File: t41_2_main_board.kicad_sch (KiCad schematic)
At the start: 18 parts, among them IC1 74HC125D, J1 Conn_02x08_Odd_Even, J2 Conn_02x05_Odd_Even, J3 Conn_02x05_Odd_Even, J4 Conn_02x05_Odd_Even, J5 Conn_02x05_Odd_Even, J6 SJ-3524-SMT, J7 SJ-3524-SMT, J8 SJ-3524-SMT, U1 Teensy4.1

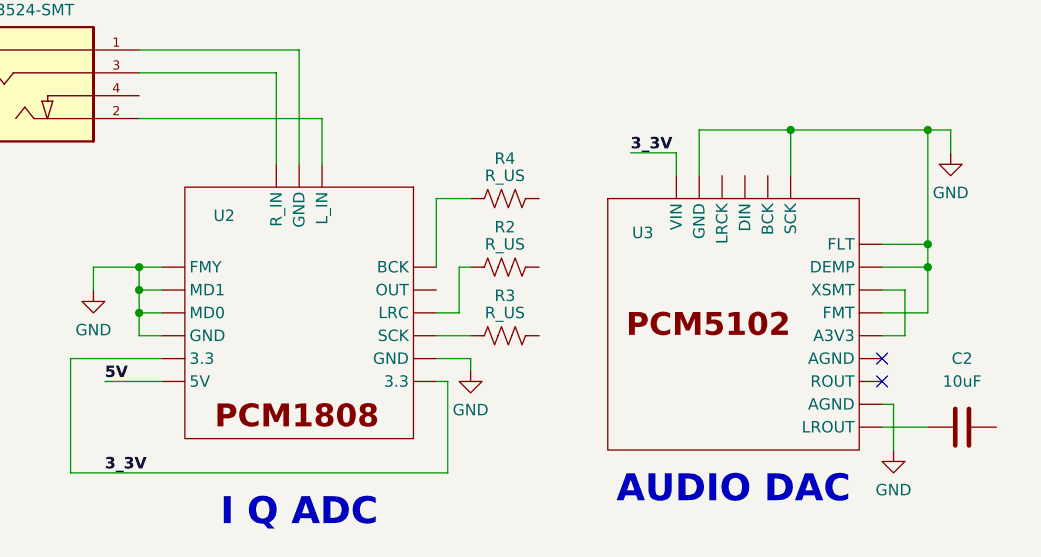
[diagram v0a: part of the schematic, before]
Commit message: Built footprints for data converters.
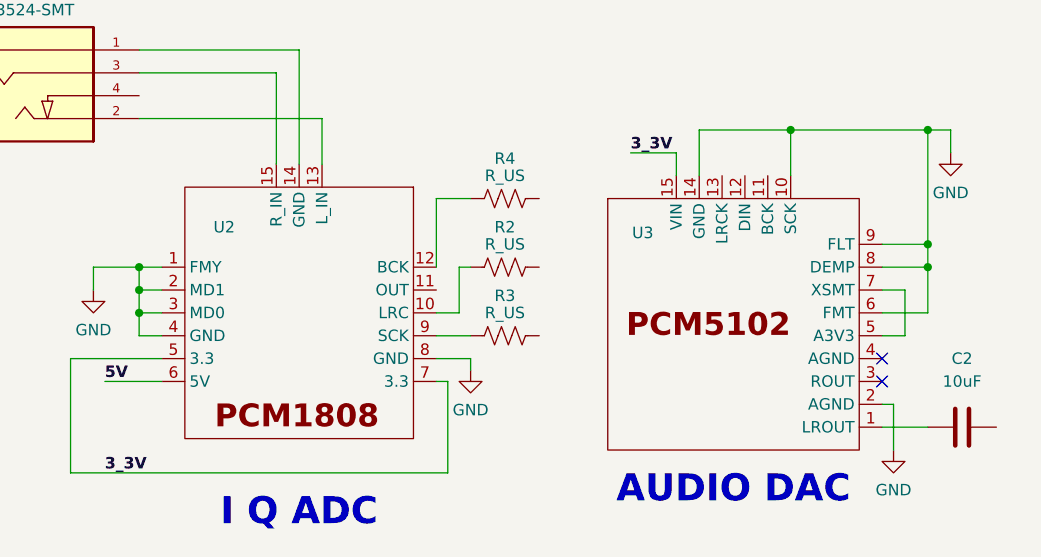
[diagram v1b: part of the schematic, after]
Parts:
- U1: footprint (none) -> teensy:Teensy41
- U2: footprint (none) -> PCM1808_module:PCM1808_module
- U3: footprint (none) -> PCM5102_module:PCM5102_module
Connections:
- net 3_3V: now also U2.5 (3.3), U2.7 (3.3), U3.15 (VIN); no longer U2. (SCK), U3. (XSMT)
- net 5V: now also U2.6 (5V); no longer U2. (SCK)
- net GND: now also U2.1 (FMY), U2.2 (MD1), U2.3 (MD0), U2.4 (GND), U2.8 (GND), U3.10 (SCK), U3.14 (GND), U3.2 (AGND), U3.6 (FMT), U3.8 (DEMP), U3.9 (FLT); no longer U2. (SCK), U3. (XSMT)
- net at R2.1: now also U2.10 (LRC); no longer U2. (SCK)
- net at J6.1: now also U2.14 (GND); no longer U2. (SCK)
- net at J6.2: now also U2.13 (L_IN); no longer U2. (SCK)
- net at J6.3: now also U2.15 (R_IN); no longer U2. (SCK)
- net at C2.1: now also U3.1 (LROUT); no longer U3. (XSMT)
- net at R4.1: now also U2.12 (BCK); no longer U2. (SCK)
- net at R3.1: now also U2.9 (SCK); no longer U2. (SCK)
- new net: U3.5 (A3V3), U3.7 (XSMT)
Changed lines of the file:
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@@
 			)
 		)
-		(property "Footprint" ""
+		(property "Footprint" "teensy:Teensy41"
 			(at 81.28 95.25 0)
 			(effects
@@
 			)
 		)
-		(property "Footprint" ""
+		(property "Footprint" "PCM5102_module:PCM5102_module"
 			(at 111.76 178.435 0)
 			(effects
@@
 			)
 		)
-		(pin ""
-		)
-		(pin ""
-		)
-		(pin ""
-		)
-		(pin ""
-		)
-		(pin ""
-		)
-		(pin ""
-		)
-		(pin ""
-		)
-		(pin ""
-		)
-		(pin ""
-		)
-		(pin ""
-		)
-		(pin ""
-		)
-		(pin ""
-		)
-		(pin ""
-		)
-		(pin ""
-		)
-		(pin ""
+		(pin "1"
+		)
+		(pin "3"
+		)
+		(pin "13"
+		)
+		(pin "2"
+		)
+		(pin "14"
+		)
+		(pin "11"
+		)
+		(pin "6"
+		)
+		(pin "7"
+		)
+		(pin "12"
+		)
+		(pin "4"
+		)
+		(pin "5"
+		)
+		(pin "10"
+		)
+		(pin "15"
+		)
+		(pin "9"
+		)
+		(pin "8"
 		)
 		(instances
@@
 	(symbol
 		(lib_id "PCM1808_module:PCM1808_module")
-		(at 63.5 178.435 270)
+		(at 63.5 177.165 0)
 		(unit 1)
 		(exclude_from_sim no)
@@
 		(dnp no)
 		(property "Reference" "U2"
-			(at 53.975 166.37 90)
+			(at 53.975 167.64 0)
 			(effects
 				(font
@@
 		)
 		(property "Value" "~"
-			(at 67.31 212.725 0)
+			(at 97.79 173.355 0)
 			(effects
 				(font
@@
 			)
 		)
-		(property "Footprint" ""
-			(at 63.5 178.435 0)
+		(property "Footprint" "PCM1808_module:PCM1808_module"
+			(at 63.5 177.165 0)
 			(effects
 				(font
@@
 		)
 		(property "Datasheet" ""
-			(at 63.5 178.435 0)
+			(at 63.5 177.165 0)
 			(effects
 				(font
@@
 		)
 		(property "Description" ""
-			(at 63.5 178.435 0)
-			(effects
-				(font
-					(size 1.27 1.27)
-				)
-				(hide yes)
-			)
-		)
-		(pin ""
-		)
-		(pin ""
-		)
-		(pin ""
-		)
-		(pin ""
-		)
-		(pin ""
-		)
-		(pin ""
-		)
-		(pin ""
-		)
-		(pin ""
-		)
-		(pin ""
-		)
-		(pin ""
-		)
-		(pin ""
-		)
-		(pin ""
-		)
-		(pin ""
-		)
-		(pin ""
-		)
-		(pin ""
-		)
-		(instances
+			(at 63.5 177.165 0)
+			(effects
+				(font
+					(size 1.27 1.27)
+				)
+				(hide yes)
+			)
+		)
+		(pin "4"
+		)
+		(pin "7"
+		)
+		(pin "1"
+		)
+		(pin "14"
+		)
+		(pin "9"
+		)
+		(pin "2"
+		)
+		(pin "11"
+		)
+		(pin "15"
+		)
+		(pin "5"
+		)
+		(pin "6"
+		)
+		(pin "3"
+		)
+		(pin "10"
+		)
+		(pin "8"
+		)
+		(pin "13"
+		)
+		(pin "12"
+		)
+		(instances

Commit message: Schematic nearing completion.
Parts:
- added C10, C11, C12, C13, C14, C15, C3, C7, C8, C9: 470pF, symbol Device:C_Small
- added C4, C5, C6: C_Small, symbol Device:C_Small
- added FB1, FB2, FB3, FB4, FB5: FerriteBead, symbol Device:FerriteBead_Small
- added J10, J12: SJ-3524-SMT, Connector_Audio:Jack_3.5mm_CUI_SJ-3524-SMT_Horizontal, symbol SJ-3524-SMT:SJ-3524-SMT
- added J11: B2B-XH-A_LF__SN_, digikey-footprints:PinHeader_1x2_P2.5mm_Drill1.1mm, symbol dk_Rectangular-Connectors-Headers-Male-Pins:B2B-XH-A_LF__SN_
- added J13, J9: B3B-XH-A_LF__SN_, digikey-footprints:PinHeader_1x3_P2.5mm_Drill1.1mm, symbol dk_Rectangular-Connectors-Headers-Male-Pins:B3B-XH-A_LF__SN_
- added J15: B4B-XH-A_LF__SN_, digikey-footprints:PinHeader_1x4_P2.5mm_Drill1.1mm, symbol dk_Rectangular-Connectors-Headers-Male-Pins:B4B-XH-A_LF__SN_
- IC1: footprint SOIC14 -> Package_SO:SOIC-14_3.9x8.7mm_P1.27mm
- J1: footprint (none) -> Connector_IDC:IDC-Header_2x08_P2.54mm_Vertical
- J2, J3, J4, J5: footprint (none) -> Connector_IDC:IDC-Header_2x05_P2.54mm_Vertical
- J6, J7, J8: footprint CUI_SJ-3524-SMT -> Connector_Audio:Jack_3.5mm_CUI_SJ-3524-SMT_Horizontal
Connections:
- net 5V is gone; now on net 5V_FIL: U2.6 (5V)
- net CS: now also U1.12 (10_CS_MQSR)
- net GND: now also J2.1 (Pin_1), J2.2 (Pin_2), J3.9 (Pin_9), J4.1 (Pin_1), J4.2 (Pin_2), J6.1, J8.1, U1.34 (GND), U1.47 (GND), U2.14 (GND), C3.2, C4.2, C5.2, C6.2, C7.1, C8.1, J10.1, J12.1, J13.2
- net MISO: now also IC1.6, U1.14 (12_MISO_MQSL)
- net MOSI: now also U1.13 (11_MOSI_CTX1); no longer IC1.3, J5.4 (Pin_4)
- net at J4.5 (Pin_5): now also U1.38 (16_A2_RX4_SCL1)
- net at J4.6 (Pin_6): now also U1.36 (14_A0_TX3_SPDIF_OUT)
- net at J4.7 (Pin_7): now also U1.39 (17_A3_TX4_SDA1)
- net at J4.8 (Pin_8): now also U1.37 (15_A1_RX3_SPDIF_IN)
- net at J7.1: now also J9.2
- net at J7.2: now also J9.1
- net at J7.3: now also J9.3
- net at J8.2: now also J11.1
- net at J8.3: now also J11.2
- net RESET: now reaches J1.1 (Pin_1)
- net RESET: now also U1.2 (0_RX1_CRX2_CS1)
- net 5V_IN: now reaches J1.10 (Pin_10)
- net 5V_IN: now also J1.9 (Pin_9), FB2.1
- net TXRX: now reaches J1.2 (Pin_2)
- net SDA: now reaches J1.3 (Pin_3)
- net SDA: now also J3.7 (Pin_7), U1.40 (18_A4_SDA)
- net SCL: now reaches J1.4 (Pin_4)
- net SCL: now also J3.8 (Pin_8), U1.41 (19_A5_SCL)
- net 12V_IN: now reaches J1.5 (Pin_5)
- net 12V_IN: now also J1.6 (Pin_6), FB1.1
- net 20MFILTER: now reaches U1.20 (28_RX7)
- net 20MFILTER: now also J3.3 (Pin_3)
- net 15MFILTER: now reaches U1.21 (29_TX7)
- net 15MFILTER: now also J3.4 (Pin_4)
- net 80MFILTER: now reaches U1.22 (30_CRX3)
- net 80MFILTER: now also J3.1 (Pin_1)
- net 40MFILTER: now reaches U1.23 (31_CTX3)
- net 40MFILTER: now also J3.2 (Pin_2)
- net DIN: now reaches U1.24 (32_OUT1B)
- net DIN: now also U3.12 (DIN)
- net KEY2: now reaches U1.27 (35_TX8)
- net KEY2: now also C8.2, FB5.1
- net KEY1: now reaches U1.28 (36_CS)
- net KEY1: now also C7.2, FB4.1
- net PTT: now reaches U1.29 (37_CS)
- net MUTE: now reaches U1.30 (38_CS1_IN1)
- net SWITCH_MATRIX: now reaches U1.31 (39_MISO1_OUT1A)
- net SWITCH_MATRIX: now also C3.1, J13.1
- net CLK0: now reaches U1.35 (13_SCK_LED)
- net at U1.4 (2_OUT2): now also J2.5 (Pin_5)
- net LRCLK: now reaches U1.42 (20_A6_TX5_LRCLK1)
- net LRCLK: now also U1.8 (6_OUT1D)
- net BCLK: now reaches U1.43 (21_A7_RX5_BCLK1)
- net RXTX: now reaches U1.44 (22_A8_CTX1)
- net RXTX: now also J3.10 (Pin_10)
- net MCLK: now reaches U1.45 (23_A9_CRX1_MCLK1)
- net 3V3: now reaches U1.46 (3V3)
- net 3V3: now also J13.3
- net 5V_FIL: now reaches U1.48 (VIN)
- net 5V_FIL: now also C5.1, FB2.2
- net at U1.5 (3_LRCLK2): now also J2.7 (Pin_7)
- net at U1.6 (4_BCLK2): now also J2.6 (Pin_6)
- net at U1.7 (5_IN2): now also J2.8 (Pin_8)
- net at C2.2: now also J12.2
- net CLK0_OUT: now reaches IC1.8, J5.3 (Pin_3)
- net 3_3V renamed 3_3V_FIL
- net 3_3V_FIL: now also C6.1, FB3.2; no longer J1.13 (Pin_13), J1.14 (Pin_14)
- new net: FB5.2, J10.3
- new net: FB4.2, J10.2
- new net 12V_FIL: C4.1, FB1.2
- new net 3_3V_IN: FB3.1, J1.13 (Pin_13), J1.14 (Pin_14)
- new net MOSI_OUT: IC1.3, J5.4 (Pin_4)
- no-connect marks 4 -> 28
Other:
- note added: "AUDIO ENABLE"
- note added: "AUDIO OUT AND"
- note added: "AUDIO OUTPUT"
- note added: "CHECK IQ CONNECTIONS!"
- note added: "CHECK KEY CONNECTIONS!"
- note added: "CHECK MIC CONNECTIONS!"
- note added: "ENCODERS"
- note added: "POWER"
- note added: "Put power on this connector so 16 pin not required?"
- note added: "RECEIVER IQ ADC"
- note added: "TO KEY"
- note added: "TO SWITCH MATRIX"
- note added: "TUNE-FILTER"
- note added: "VOLUME-FINETUNE"
- note removed: "I Q ADC"
- moved on the sheet: C1, C2, IC1, J1, J2, J3, J4, J5, J7, J8, R1, U1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

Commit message: Placement done.
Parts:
- removed C14: 470pF, symbol Device:C_Small
- removed R1: R_US, symbol Device:R_US
- added C16: 470pF, Capacitor_SMD:C_1206_3216Metric, symbol Device:C_Small
- added FB10, FB6, FB7, FB8, FB9: FerriteBead, Inductor_SMD:L_1206_3216Metric, symbol Device:FerriteBead_Small
- C1, C10, C11, C12, C13, C15, C2, C3, C7, C8, C9: footprint (none) -> Capacitor_SMD:C_1206_3216Metric
- C4, C5, C6: value C_Small -> 0.1uF; footprint (none) -> Capacitor_SMD:C_1206_3216Metric
- FB1, FB2, FB3, FB4, FB5: footprint (none) -> Inductor_SMD:L_1206_3216Metric
- J10, J12, J6, J7, J8: footprint Connector_Audio:Jack_3.5mm_CUI_SJ-3524-SMT_Horizontal -> SJ-3524-SMT:CUI_SJ-3524-SMT
- R2, R3, R4: value R_US -> 100; footprint (none) -> Resistor_SMD:R_1206_3216Metric
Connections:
- net BCLK is gone; now on net BCK: U1.43 (21_A7_RX5_BCLK1)
- net 15MFILTER: now also C13.2, FB9.2; no longer J3.4 (Pin_4)
- net 20MFILTER: now also C11.2, FB7.1; no longer J3.3 (Pin_3)
- net 3_3V_FIL: now also IC1.14
- net 40MFILTER: now also C12.2, FB8.2; no longer J3.2 (Pin_2)
- net 80MFILTER: now also C10.2, FB6.1; no longer J3.1 (Pin_1)
- net CLK0: now also IC1.9
- net CS: now also IC1.1, IC1.10, IC1.4
- net GND: now also C10.1, C11.1, C12.1, C13.1, C15.2, C9.1, J15.2, J15.4, C16.1
- net LRCLK: now also R2.2, U3.13 (LRCK); no longer U1.8 (6_OUT1D)
- net MCLK: now also R3.2
- net MISO: no longer J5.5 (Pin_5)
- net MISO_IN: now also IC1.5, J5.5 (Pin_5)
- net MOSI: now also IC1.2
- net MUTE: now also J15.1, C16.2
- net PTT: now also J11.1, J8.2
- net RXTX: now also C15.1, FB10.2; no longer J3.10 (Pin_10), U1.44 (22_A8_CTX1)
- net TXRX: now also U1.44 (22_A8_CTX1)
- net at C2.2, J12.2: now also C9.2, J15.3
- net BCK: now reaches U3.11 (BCK)
- net BCK: now also R4.2
- net OUT: now reaches U2.11 (OUT)
- net OUT: now also U1.8 (6_OUT1D)
- new net: FB7.2, J3.3 (Pin_3)
- new net: FB10.1, J3.10 (Pin_10)
- new net: FB9.1, J3.4 (Pin_4)
- new net: FB8.1, J3.2 (Pin_2)
- new net: FB6.2, J3.1 (Pin_1)
- no-connect marks 28 -> 57
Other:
- note added: "Terminal block for 12v auxiliary?"
- note removed: "CHECK IQ CONNECTIONS!"
- moved on the sheet: C10, C11, C13, C15, C9, J15, J6, J9, R2, R3, R4, U2

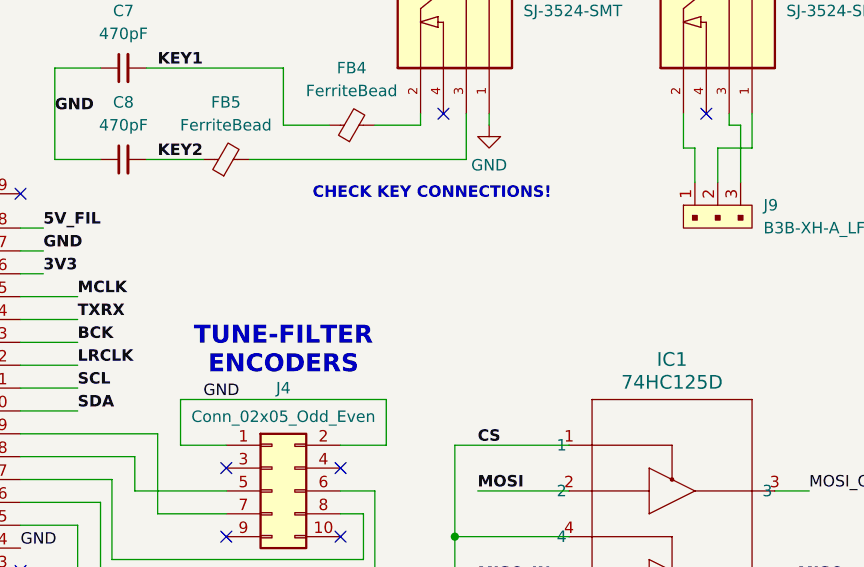
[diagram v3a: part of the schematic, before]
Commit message: Audio routing is not good, starting another branch.
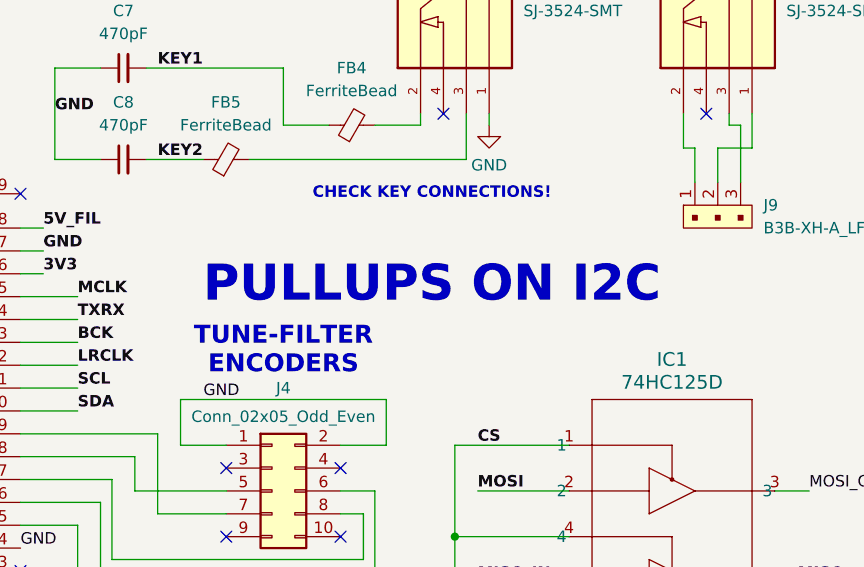
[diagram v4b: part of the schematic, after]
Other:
- note added: "PULLUPS ON I2C"
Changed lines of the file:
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@@
+		)
+	)
+	(text "PULLUPS ON I2C"
+		(exclude_from_sim no)
+		(at 179.07 62.23 0)
+		(effects
+			(font
+				(size 4 4)
+				(thickness 0.8)
+				(bold yes)
+			)
 		)
 	)

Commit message: To fab.
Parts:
- added C14: 2.2nF, Capacitor_SMD:C_1206_3216Metric, symbol Device:C
- added J14: B2B-XH-A_LF__SN_, digikey-footprints:PinHeader_1x2_P2.5mm_Drill1.1mm, symbol dk_Rectangular-Connectors-Headers-Male-Pins:B2B-XH-A_LF__SN_
- added J16: B3B-XH-A_LF__SN_, digikey-footprints:PinHeader_1x3_P2.5mm_Drill1.1mm, symbol dk_Rectangular-Connectors-Headers-Male-Pins:B3B-XH-A_LF__SN_
- added R1: 470, Resistor_SMD:R_1206_3216Metric, symbol Device:R_US
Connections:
- net 3_3V_FIL: now also U3.5 (A3V3), U3.7 (XSMT), J16.1
- net 5V_FIL: now also J16.3
- net GND: now also U3.4 (AGND), C14.1, J14.2
- net at J4.6 (Pin_6): now also U1.33 (41_A17); no longer U1.36 (14_A0_TX3_SPDIF_OUT)
- net at C2.1: now also C14.2, R1.2; no longer U3.1 (LROUT)
- net DISP_PWR: now reaches J5.7 (Pin_7)
- net DISP_PWR: now also J5.8 (Pin_8), J16.2
- new net: R1.1, U3.1 (LROUT)
- new net SPDIF_OUT: J14.1, U1.36 (14_A0_TX3_SPDIF_OUT)
- no-connect marks 57 -> 53
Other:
- note added: "DISPLAY POWER JUMPER"
- note removed: "CHECK KEY CONNECTIONS!"
- note removed: "CHECK MIC CONNECTIONS!"
- note removed: "Terminal block for 12v auxiliary?"
- moved on the sheet: C2
